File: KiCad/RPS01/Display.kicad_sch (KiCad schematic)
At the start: 5 parts, among them J22 RGB LED, J22 i2c Display Header

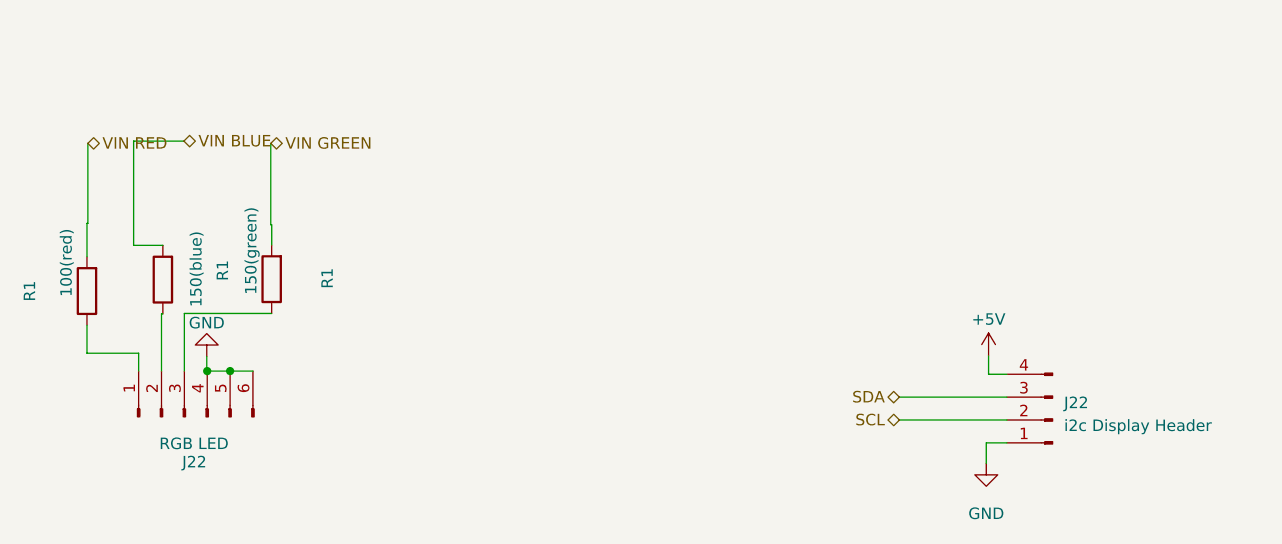
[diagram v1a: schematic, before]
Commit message: Finished most of the Schematics. Needs polishing
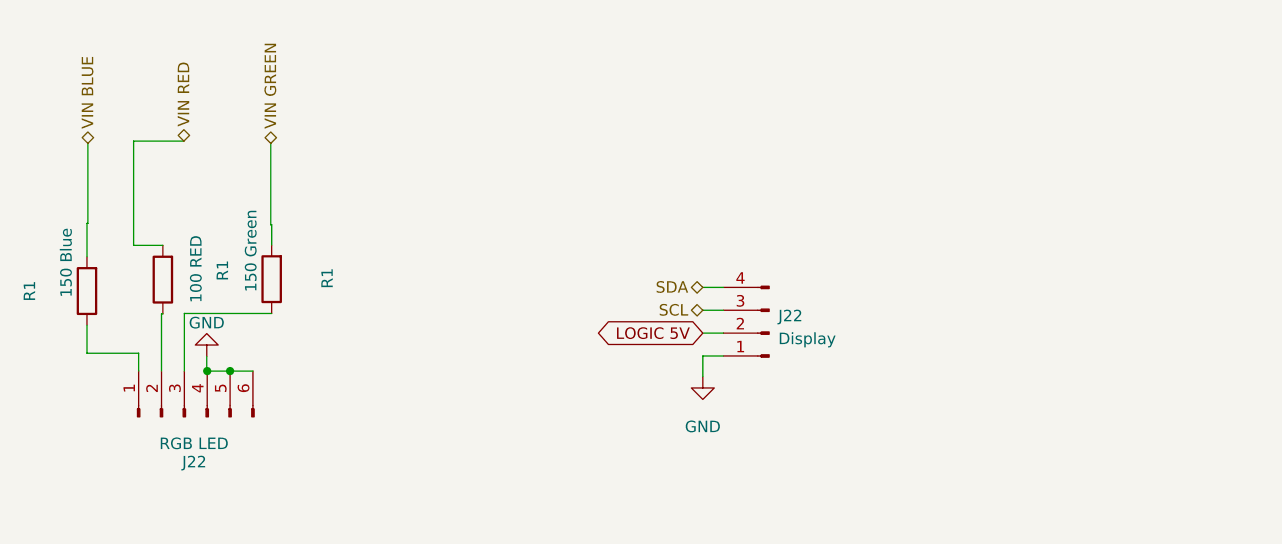
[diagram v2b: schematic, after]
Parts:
- J22: value i2c Display Header -> Display
- R1: value 100(red) -> 150 Blue
- R1: value 150(blue) -> 100 RED
- R1: value 150(green) -> 150 Green
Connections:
- net +5V is gone; now on net SDA: J22.4 (Pin_4)
- net SCL: now also J22.3 (Pin_3); no longer J22.2 (Pin_2)
- net SDA: no longer J22.3 (Pin_3)
- net VIN BLUE: now also R1.2; no longer R1.2
- net VIN RED: now also R1.2; no longer R1.2
- new net LOGIC 5V: J22.2 (Pin_2)
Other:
- moved on the sheet: J22
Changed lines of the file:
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@@
-    (stroke (width 0) (type default))
-  )
-  (wire (pts (xy 226.568 62.23) (xy 226.568 64.262))
-    (stroke (width 0) (type default))
-  )
-  (wire (pts (xy 216.662 69.342) (xy 228.6 69.342))
     (stroke (width 0) (type default))
   )
@@
     (stroke (width 0) (type default))
   )
+  (wire (pts (xy 194.818 57.15) (xy 197.104 57.15))
+    (stroke (width 0) (type default))
+  )
   (wire (pts (xy 139.7508 63.9064) (xy 142.2908 63.9064))
     (stroke (width 0) (type default))
@@
     (stroke (width 0) (type default))
   )
-  (wire (pts (xy 228.6 64.262) (xy 226.568 64.262))
+  (wire (pts (xy 194.818 59.69) (xy 197.104 59.69))
     (stroke (width 0) (type default))
   )
@@
     (stroke (width 0) (type default))
   )
-  (wire (pts (xy 228.6 71.882) (xy 226.314 71.882))
-    (stroke (width 0) (type default))
-  )
-  (wire (pts (xy 226.314 71.882) (xy 226.314 74.168))
+  (wire (pts (xy 197.104 62.23) (xy 194.818 62.23))
+    (stroke (width 0) (type default))
+  )
+  (wire (pts (xy 194.818 62.23) (xy 194.818 64.516))
     (stroke (width 0) (type default))
   )
@@
     (stroke (width 0) (type default))
   )
-  (wire (pts (xy 216.662 66.802) (xy 228.6 66.802))
+  (wire (pts (xy 194.818 54.61) (xy 197.104 54.61))
     (stroke (width 0) (type default))
   )
@@
     (stroke (width 0) (type default))
   )
-  (hierarchical_label "VIN RED" (shape bidirectional) (at 126.492 38.608 0) (fields_autoplaced)
+  (global_label "LOGIC 5V" (shape bidirectional) (at 194.818 59.69 180) (fields_autoplaced)
+    (effects (font (size 1.27 1.27)) (justify right))
+    (property "Intersheetrefs" "${INTERSHEET_REFS}" (at 182.0318 59.69 0)
+      (effects (font (size 1.27 1.27)) (justify right) hide)
+    )
+  )
+  (hierarchical_label "VIN BLUE" (shape bidirectional) (at 126.492 38.608 90) (fields_autoplaced)
     (effects (font (size 1.27 1.27)) (justify left))
   )
-  (hierarchical_label "SCL" (shape bidirectional) (at 216.662 69.342 180) (fields_autoplaced)
+  (hierarchical_label "SCL" (shape bidirectional) (at 194.818 57.15 180) (fields_autoplaced)
     (effects (font (size 1.27 1.27)) (justify right))
   )
-  (hierarchical_label "SDA" (shape bidirectional) (at 216.662 66.802 180) (fields_autoplaced)
+  (hierarchical_label "SDA" (shape bidirectional) (at 194.818 54.61 180) (fields_autoplaced)
     (effects (font (size 1.27 1.27)) (justify right))
   )
-  (hierarchical_label "VIN BLUE" (shape bidirectional) (at 137.16 38.354 0) (fields_autoplaced)
+  (hierarchical_label "VIN RED" (shape bidirectional) (at 137.16 38.354 90) (fields_autoplaced)
     (effects (font (size 1.27 1.27)) (justify left))
   )
-  (hierarchical_label "VIN GREEN" (shape bidirectional) (at 146.812 38.608 0) (fields_autoplaced)
+  (hierarchical_label "VIN GREEN" (shape bidirectional) (at 146.812 38.608 90) (fields_autoplaced)
     (effects (font (size 1.27 1.27)) (justify left))
   )
-  (symbol (lib_id "Connector:Conn_01x04_Pin") (at 233.68 69.342 180) (unit 1)
+  (symbol (lib_id "Connector:Conn_01x04_Pin") (at 202.184 59.69 180) (unit 1)
     (in_bom yes) (on_board yes) (dnp no) (fields_autoplaced)
-    (property "Reference" "J22" (at 234.95 67.437 0)
+    (property "Reference" "J22" (at 203.2 57.785 0)
       (effects (font (size 1.27 1.27)) (justify right))
     )
-    (property "Value" "i2c Display Header" (at 234.95 69.977 0)
+    (property "Value" "Display" (at 203.2 60.325 0)
       (effects (font (size 1.27 1.27)) (justify right))
     )
-    (property "Footprint" "SSD1306:128x64OLED" (at 233.68 69.342 0)
-      (effects (font (size 1.27 1.27)) hide)
-    )
-    (property "Datasheet" "~" (at 233.68 69.342 0)
+    (property "Footprint" "SSD1306:128x64OLED" (at 202.184 59.69 0)
+      (effects (font (size 1.27 1.27)) hide)
+    )
+    (property "Datasheet" "~" (at 202.184 59.69 0)
       (effects (font (size 1.27 1.27)) hide)
     )
@@
         )
         (path "/14930f15-c0a0-4b55-93e6-b112548415f6/66639be3-b7af-4c3b-a889-0b5ac725a84a"
-          (reference "J13") (unit 1)
-        )
-      )
-    )
-  )
-  (symbol (lib_id "power:GND") (at 226.314 74.168 0) (unit 1)
+          (reference "J15") (unit 1)
+        )
+      )
+    )
+  )
+  (symbol (lib_id "power:GND") (at 194.818 64.516 0) (unit 1)
     (in_bom yes) (on_board yes) (dnp no) (fields_autoplaced)
-    (property "Reference" "#PWR031" (at 226.314 80.518 0)
-      (effects (font (size 1.27 1.27)) hide)
-    )
-    (property "Value" "GND" (at 226.314 79.756 0)
-      (effects (font (size 1.27 1.27)))
-    )
-    (property "Footprint" "" (at 226.314 74.168 0)
-      (effects (font (size 1.27 1.27)) hide)
-    )
-    (property "Datasheet" "" (at 226.314 74.168 0)
+    (property "Reference" "#PWR031" (at 194.818 70.866 0)
+      (effects (font (size 1.27 1.27)) hide)
+    )
+    (property "Value" "GND" (at 194.818 70.104 0)
+      (effects (font (size 1.27 1.27)))
+    )
+    (property "Footprint" "" (at 194.818 64.516 0)
+      (effects (font (size 1.27 1.27)) hide)
+    )
+    (property "Datasheet" "" (at 194.818 64.516 0)
       (effects (font (size 1.27 1.27)) hide)
     )
@@
         )
         (path "/14930f15-c0a0-4b55-93e6-b112548415f6/66639be3-b7af-4c3b-a889-0b5ac725a84a"
-          (reference "#PWR049") (unit 1)
+          (reference "#PWR050") (unit 1)
         )
       )
@@
       (effects (font (size 1.27 1.27)))
     )
-    (property "Value" "100(red)" (at 124.1044 51.8668 90)
+    (property "Value" "150 Blue" (at 124.1044 51.8668 90)
       (effects (font (size 1.27 1.27)))
     )
@@
         )
         (path "/14930f15-c0a0-4b55-93e6-b112548415f6/66639be3-b7af-4c3b-a889-0b5ac725a84a"
-          (reference "R12") (unit 1)
+          (reference "R24") (unit 1)
         )
       )
@@
         (path "/8f0e16c9-4bd2-4a25-a569-54925ece9d23"
           (reference "R2") (unit 1)
-        )
-      )
-    )
-  )
-  (symbol (lib_id "power:+5V") (at 226.568 62.23 0) (unit 1)
-    (in_bom yes) (on_board yes) (dnp no) (fields_autoplaced)
-    (property "Reference" "#PWR044" (at 226.568 66.04 0)
-      (effects (font (size 1.27 1.27)) hide)
-    )
-    (property "Value" "+5V" (at 226.568 58.166 0)
-      (effects (font (size 1.27 1.27)))
-    )
-    (property "Footprint" "" (at 226.568 62.23 0)
-      (effects (font (size 1.27 1.27)) hide)
-    )
-    (property "Datasheet" "" (at 226.568 62.23 0)
-      (effects (font (size 1.27 1.27)) hide)
-    )
-    (pin "1")
-    (instances
-      (project "rps01"
-        (path "/14930f15-c0a0-4b55-93e6-b112548415f6"
-          (reference "#PWR044") (unit 1)
-        )
-        (path "/14930f15-c0a0-4b55-93e6-b112548415f6/a2e49fe6-126d-427d-b045-54fb7f662aa7"
-          (reference "#PWR053") (unit 1)
-        )
-        (path "/14930f15-c0a0-4b55-93e6-b112548415f6/66639be3-b7af-4c3b-a889-0b5ac725a84a"
-          (reference "#PWR050") (unit 1)
         )
       )
@@
         )
         (path "/14930f15-c0a0-4b55-93e6-b112548415f6/66639be3-b7af-4c3b-a889-0b5ac725a84a"
-          (reference "J4") (unit 1)
+          (reference "J14") (unit 1)
         )
       )
@@
         )
         (path "/14930f15-c0a0-4b55-93e6-b112548415f6/66639be3-b7af-4c3b-a889-0b5ac725a84a"
-          (reference "#PWR048") (unit 1)
+          (reference "#PWR049") (unit 1)
         )
       )
@@
       (effects (font (size 1.27 1.27)))
     )
-    (property "Value" "150(blue)" (at 138.5316 52.578 90)
+    (property "Value" "100 RED" (at 138.5316 52.578 90)
       (effects (font (size 1.27 1.27)))
     )
@@
         )
         (path "/14930f15-c0a0-4b55-93e6-b112548415f6/66639be3-b7af-4c3b-a889-0b5ac725a84a"
-          (reference "R13") (unit 1)
+          (reference "R25") (unit 1)
         )
       )
@@
       (effects (font (size 1.27 1.27)))
     )
-    (property "Value" "150(green)" (at 144.6276 50.546 90)
+    (property "Value" "150 Green" (at 144.6276 50.546 90)
       (effects (font (size 1.27 1.27)))
     )
@@
         )
         (path "/14930f15-c0a0-4b55-93e6-b112548415f6/66639be3-b7af-4c3b-a889-0b5ac725a84a"
-          (reference "R14") (unit 1)
-        )
-      )
+          (reference "R26") (unit 1)
+        )
+      )

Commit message: Finished Updating Footprints and Reorganized Reference Designators
Finished Updating Footprints and Reorganized Reference Designators

Starting to work on Final PCB, except for 19V Boost. Please check Schematic for errors
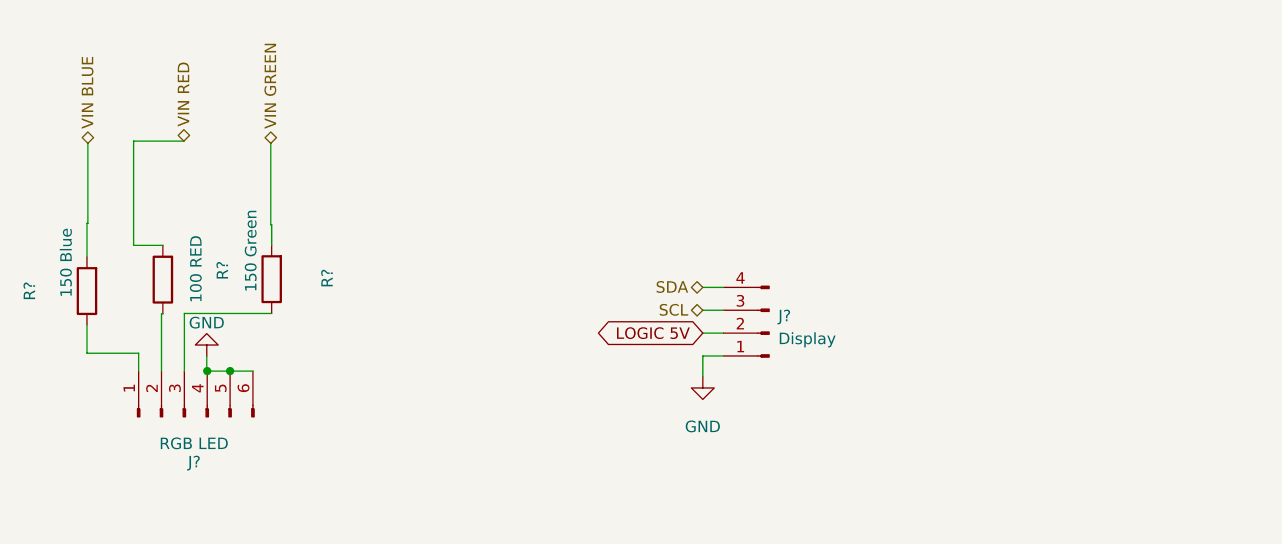
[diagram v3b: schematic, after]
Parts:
- renumbered J22 to J?, R1 to R?
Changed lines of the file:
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@@
   (symbol (lib_id "Connector:Conn_01x04_Pin") (at 202.184 59.69 180) (unit 1)
     (in_bom yes) (on_board yes) (dnp no) (fields_autoplaced)
-    (property "Reference" "J22" (at 203.2 57.785 0)
+    (property "Reference" "J?" (at 203.2 57.785 0)
       (effects (font (size 1.27 1.27)) (justify right))
     )
@@
       (project "rps01"
         (path "/14930f15-c0a0-4b55-93e6-b112548415f6"
-          (reference "J22") (unit 1)
-        )
-        (path "/14930f15-c0a0-4b55-93e6-b112548415f6/a2e49fe6-126d-427d-b045-54fb7f662aa7"
-          (reference "J23") (unit 1)
+          (reference "J?") (unit 1)
+        )
+        (path "/14930f15-c0a0-4b55-93e6-b112548415f6/a2e49fe6-126d-427d-b045-54fb7f662aa7"
+          (reference "J?") (unit 1)
         )
         (path "/14930f15-c0a0-4b55-93e6-b112548415f6/66639be3-b7af-4c3b-a889-0b5ac725a84a"
@@
   (symbol (lib_id "power:GND") (at 194.818 64.516 0) (unit 1)
     (in_bom yes) (on_board yes) (dnp no) (fields_autoplaced)
-    (property "Reference" "#PWR031" (at 194.818 70.866 0)
+    (property "Reference" "#PWR?" (at 194.818 70.866 0)
       (effects (font (size 1.27 1.27)) hide)
     )
@@
       (project "rps01"
         (path "/14930f15-c0a0-4b55-93e6-b112548415f6"
-          (reference "#PWR031") (unit 1)
-        )
-        (path "/14930f15-c0a0-4b55-93e6-b112548415f6/a2e49fe6-126d-427d-b045-54fb7f662aa7"
+          (reference "#PWR?") (unit 1)
+        )
+        (path "/14930f15-c0a0-4b55-93e6-b112548415f6/a2e49fe6-126d-427d-b045-54fb7f662aa7"
+          (reference "#PWR?") (unit 1)
+        )
+        (path "/14930f15-c0a0-4b55-93e6-b112548415f6/66639be3-b7af-4c3b-a889-0b5ac725a84a"
           (reference "#PWR052") (unit 1)
         )
-        (path "/14930f15-c0a0-4b55-93e6-b112548415f6/66639be3-b7af-4c3b-a889-0b5ac725a84a"
-          (reference "#PWR050") (unit 1)
-        )
       )
     )
@@
   (symbol (lib_id "Device:R") (at 126.3904 55.0164 180) (unit 1)
     (in_bom yes) (on_board yes) (dnp no)
-    (property "Reference" "R1" (at 120.0404 55.0164 90)
+    (property "Reference" "R?" (at 120.0404 55.0164 90)
       (effects (font (size 1.27 1.27)))
     )
@@
       (project "MCU2"
         (path "/049009a7-95d1-4ccf-a10c-7859cfd6b188"
-          (reference "R1") (unit 1)
-        )
-      )
-      (project "rps01"
-        (path "/14930f15-c0a0-4b55-93e6-b112548415f6/a2e49fe6-126d-427d-b045-54fb7f662aa7"
-          (reference "R5") (unit 1)
-        )
-        (path "/14930f15-c0a0-4b55-93e6-b112548415f6/66639be3-b7af-4c3b-a889-0b5ac725a84a"
-          (reference "R24") (unit 1)
+          (reference "R?") (unit 1)
+        )
+      )
+      (project "rps01"
+        (path "/14930f15-c0a0-4b55-93e6-b112548415f6/a2e49fe6-126d-427d-b045-54fb7f662aa7"
+          (reference "R?") (unit 1)
+        )
+        (path "/14930f15-c0a0-4b55-93e6-b112548415f6/66639be3-b7af-4c3b-a889-0b5ac725a84a"
+          (reference "R29") (unit 1)
         )
       )
       (project "M_MUC"
         (path "/8f0e16c9-4bd2-4a25-a569-54925ece9d23"
-          (reference "R2") (unit 1)
+          (reference "R?") (unit 1)
         )
       )
@@
   (symbol (lib_id "Connector:Conn_01x06_Pin") (at 137.2108 68.9864 90) (unit 1)
     (in_bom yes) (on_board yes) (dnp no)
-    (property "Reference" "J22" (at 138.3284 74.0156 90)
+    (property "Reference" "J?" (at 138.3284 74.0156 90)
       (effects (font (size 1.27 1.27)))
     )
@@
       (project "rps01"
         (path "/14930f15-c0a0-4b55-93e6-b112548415f6/a2e49fe6-126d-427d-b045-54fb7f662aa7"
-          (reference "J22") (unit 1)
+          (reference "J?") (unit 1)
         )
         (path "/14930f15-c0a0-4b55-93e6-b112548415f6/66639be3-b7af-4c3b-a889-0b5ac725a84a"
@@
   (symbol (lib_id "power:GND") (at 139.7 62.2808 180) (unit 1)
     (in_bom yes) (on_board yes) (dnp no) (fields_autoplaced)
-    (property "Reference" "#PWR015" (at 139.7 55.9308 0)
+    (property "Reference" "#PWR?" (at 139.7 55.9308 0)
       (effects (font (size 1.27 1.27)) hide)
     )
@@
       (project "MCU2"
         (path "/049009a7-95d1-4ccf-a10c-7859cfd6b188"
-          (reference "#PWR015") (unit 1)
-        )
-      )
-      (project "rps01"
-        (path "/14930f15-c0a0-4b55-93e6-b112548415f6/a2e49fe6-126d-427d-b045-54fb7f662aa7"
-          (reference "#PWR013") (unit 1)
-        )
-        (path "/14930f15-c0a0-4b55-93e6-b112548415f6/66639be3-b7af-4c3b-a889-0b5ac725a84a"
-          (reference "#PWR049") (unit 1)
+          (reference "#PWR?") (unit 1)
+        )
+      )
+      (project "rps01"
+        (path "/14930f15-c0a0-4b55-93e6-b112548415f6/a2e49fe6-126d-427d-b045-54fb7f662aa7"
+          (reference "#PWR?") (unit 1)
+        )
+        (path "/14930f15-c0a0-4b55-93e6-b112548415f6/66639be3-b7af-4c3b-a889-0b5ac725a84a"
+          (reference "#PWR051") (unit 1)
         )
       )
@@
   (symbol (lib_id "Device:R") (at 134.8232 53.7464 180) (unit 1)
     (in_bom yes) (on_board yes) (dnp no)
-    (property "Reference" "R1" (at 141.478 52.7304 90)
+    (property "Reference" "R?" (at 141.478 52.7304 90)
       (effects (font (size 1.27 1.27)))
     )
@@
       (project "MCU2"
         (path "/049009a7-95d1-4ccf-a10c-7859cfd6b188"
-          (reference "R1") (unit 1)
-        )
-      )
-      (project "rps01"
-        (path "/14930f15-c0a0-4b55-93e6-b112548415f6/a2e49fe6-126d-427d-b045-54fb7f662aa7"
-          (reference "R4") (unit 1)
-        )
-        (path "/14930f15-c0a0-4b55-93e6-b112548415f6/66639be3-b7af-4c3b-a889-0b5ac725a84a"
-          (reference "R25") (unit 1)
+          (reference "R?") (unit 1)
+        )
+      )
+      (project "rps01"
+        (path "/14930f15-c0a0-4b55-93e6-b112548415f6/a2e49fe6-126d-427d-b045-54fb7f662aa7"
+          (reference "R?") (unit 1)
+        )
+        (path "/14930f15-c0a0-4b55-93e6-b112548415f6/66639be3-b7af-4c3b-a889-0b5ac725a84a"
+          (reference "R30") (unit 1)
         )
       )
       (project "M_MUC"
         (path "/8f0e16c9-4bd2-4a25-a569-54925ece9d23"
-          (reference "R2") (unit 1)
+          (reference "R?") (unit 1)
         )
       )
@@
   (symbol (lib_id "Device:R") (at 146.9136 53.6956 180) (unit 1)
     (in_bom yes) (on_board yes) (dnp no)
-    (property "Reference" "R1" (at 153.1112 53.594 90)
+    (property "Reference" "R?" (at 153.1112 53.594 90)
       (effects (font (size 1.27 1.27)))
     )
@@
       (project "MCU2"
         (path "/049009a7-95d1-4ccf-a10c-7859cfd6b188"
-          (reference "R1") (unit 1)
-        )
-      )
-      (project "rps01"
-        (path "/14930f15-c0a0-4b55-93e6-b112548415f6/a2e49fe6-126d-427d-b045-54fb7f662aa7"
-          (reference "R6") (unit 1)
-        )
-        (path "/14930f15-c0a0-4b55-93e6-b112548415f6/66639be3-b7af-4c3b-a889-0b5ac725a84a"
-          (reference "R26") (unit 1)
+          (reference "R?") (unit 1)
+        )
+      )
+      (project "rps01"
+        (path "/14930f15-c0a0-4b55-93e6-b112548415f6/a2e49fe6-126d-427d-b045-54fb7f662aa7"
+          (reference "R?") (unit 1)
+        )
+        (path "/14930f15-c0a0-4b55-93e6-b112548415f6/66639be3-b7af-4c3b-a889-0b5ac725a84a"
+          (reference "R31") (unit 1)
         )
       )
       (project "M_MUC"
         (path "/8f0e16c9-4bd2-4a25-a569-54925ece9d23"
-          (reference "R2") (unit 1)
-        )
-      )
+          (reference "R?") (unit 1)
+        )
+      )
